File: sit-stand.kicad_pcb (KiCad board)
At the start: 2 copper layers, 160 x 50.8 mm, 63 parts, among them J1 USB_OTG, J2 CONN_02X03, J3 CONN_01X04, J4 CONN_01X16, J5 CONN_01X06, J6 CONN_02X04, U1 APA102, U10 APA102, U11 APA102, U12 APA102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

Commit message: clean up board
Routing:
- net +5V: track 453.1 -> 499.7 mm
- net GND: track 578.4 -> 573.6 mm, vias 24 -> 22
- net USB_D-: track 90.0 -> 93.9 mm
- net USB_ID: track 79.2 -> 76.9 mm
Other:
- board size 160 x 50.8 mm -> 158.8 x 50.8 mm

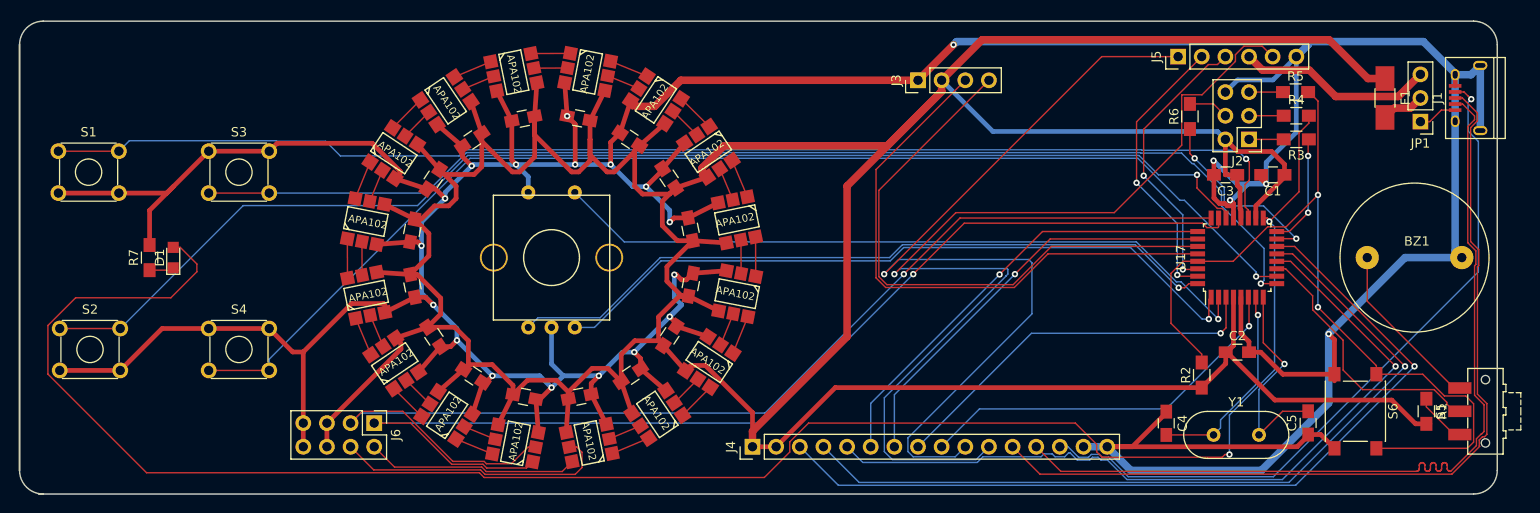
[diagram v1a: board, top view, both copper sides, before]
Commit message: shift oled and reroute led power
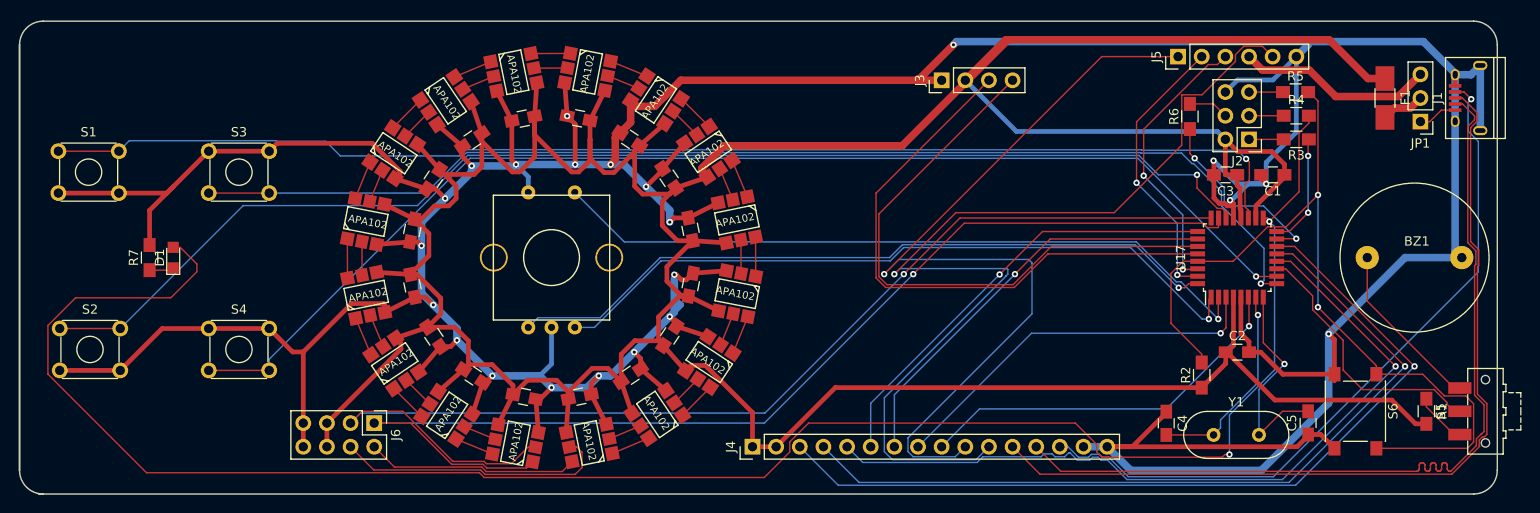
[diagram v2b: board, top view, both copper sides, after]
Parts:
- moved J3 2.54 mm to (168.9, 44.5)
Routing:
- net +5V: track 499.7 -> 456.6 mm
- net GND: track 573.6 -> 586.1 mm
- net OLED_SCL: track 61.7 -> 62.7 mm
- net OLED_SDA: track 62.3 -> 63.4 mm
- net Net-(S5-Pad2): track 28.9 -> 28.3 mm

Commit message: use thicker led power traces
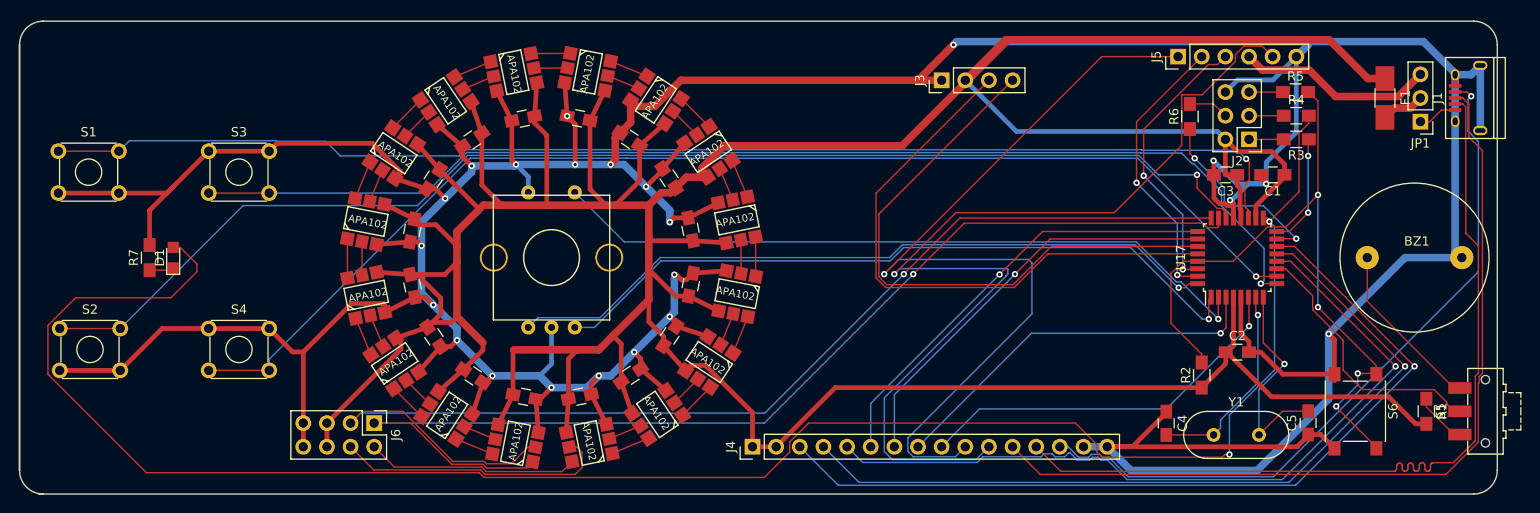
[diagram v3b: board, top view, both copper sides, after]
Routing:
- net +5V: track 456.6 -> 483.3 mm
- net RESET: track 91.1 -> 77.3 mm, vias 2 -> 4
- net GND: track 586.1 -> 573.7 mm
- net USB_D+: track 93.1 -> 91.5 mm
- net USB_D-: track 93.9 -> 92.3 mm

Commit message: added mounting holes
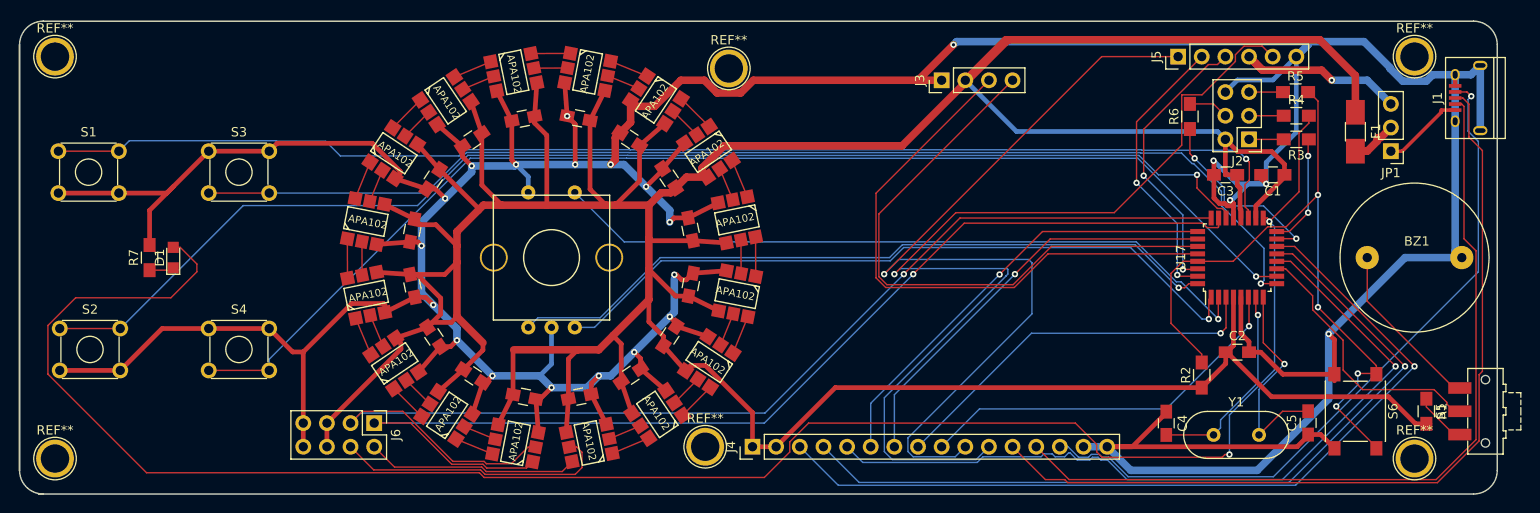
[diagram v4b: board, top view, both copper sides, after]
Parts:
- added REF**: 1pin, Connectors:1pin, F.Cu at (219.7, 41.9)
- added REF**: 1pin, Connectors:1pin, F.Cu at (143.5, 83.8)
- added REF**: 1pin, Connectors:1pin, F.Cu at (219.7, 85.1)
- added REF**: 1pin, Connectors:1pin, F.Cu at (146.1, 43.2)
- added REF**: 1pin, Connectors:1pin, F.Cu at (73.7, 85.1)
- added REF**: 1pin, Connectors:1pin, F.Cu at (73.7, 41.9)
- moved F1 4.82 mm to (213.4, 50.0)
- moved JP1 4.49 mm to (217.2, 52.1)
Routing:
- net Net-(J1-Pad1): track 4.24 -> 8.87 mm
- net USB_D-: track 92.3 -> 88.6 mm
- net SER_VCC: track 21.2 -> 19.4 mm, vias 0 -> 1
- net GND: track 573.7 -> 575.4 mm
- net USB_D+: track 91.5 -> 92.3 mm
- net +5V: track 483.3 -> 483.9 mm

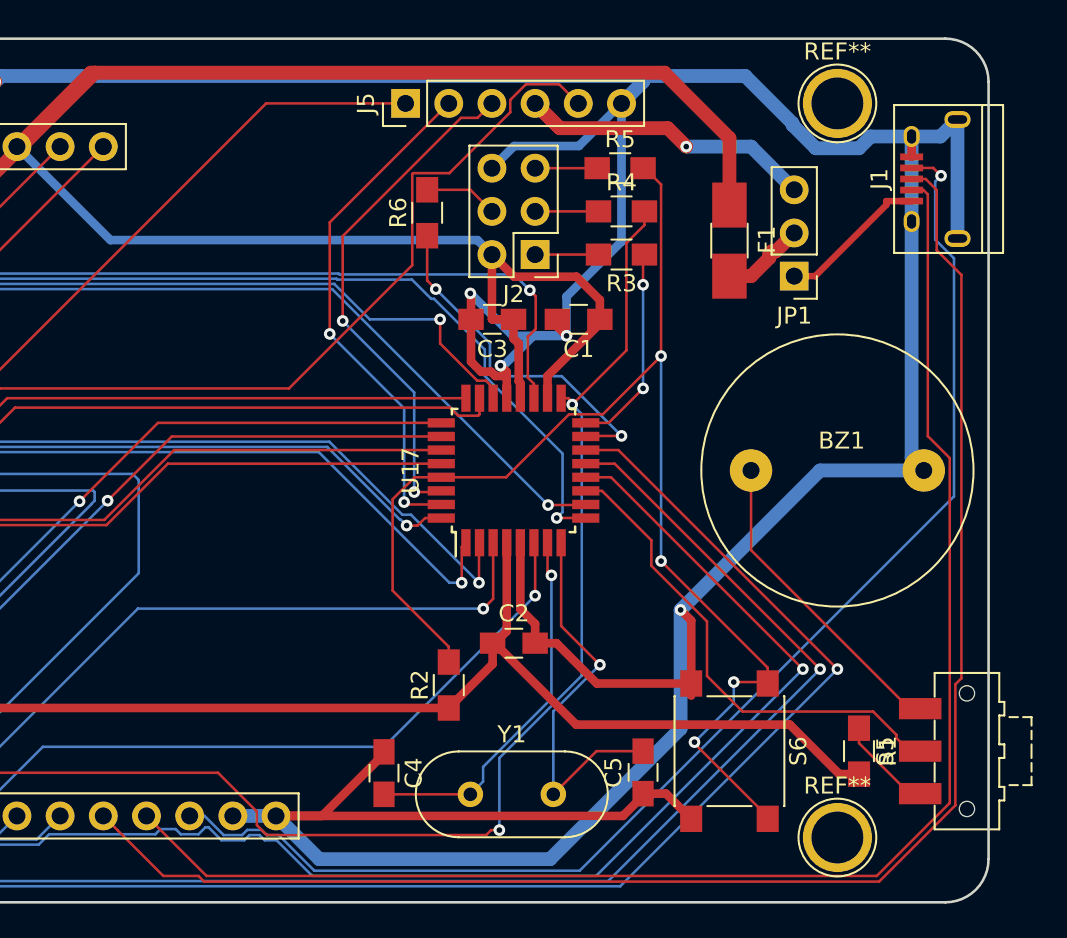
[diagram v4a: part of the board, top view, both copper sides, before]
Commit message: fixed differentials
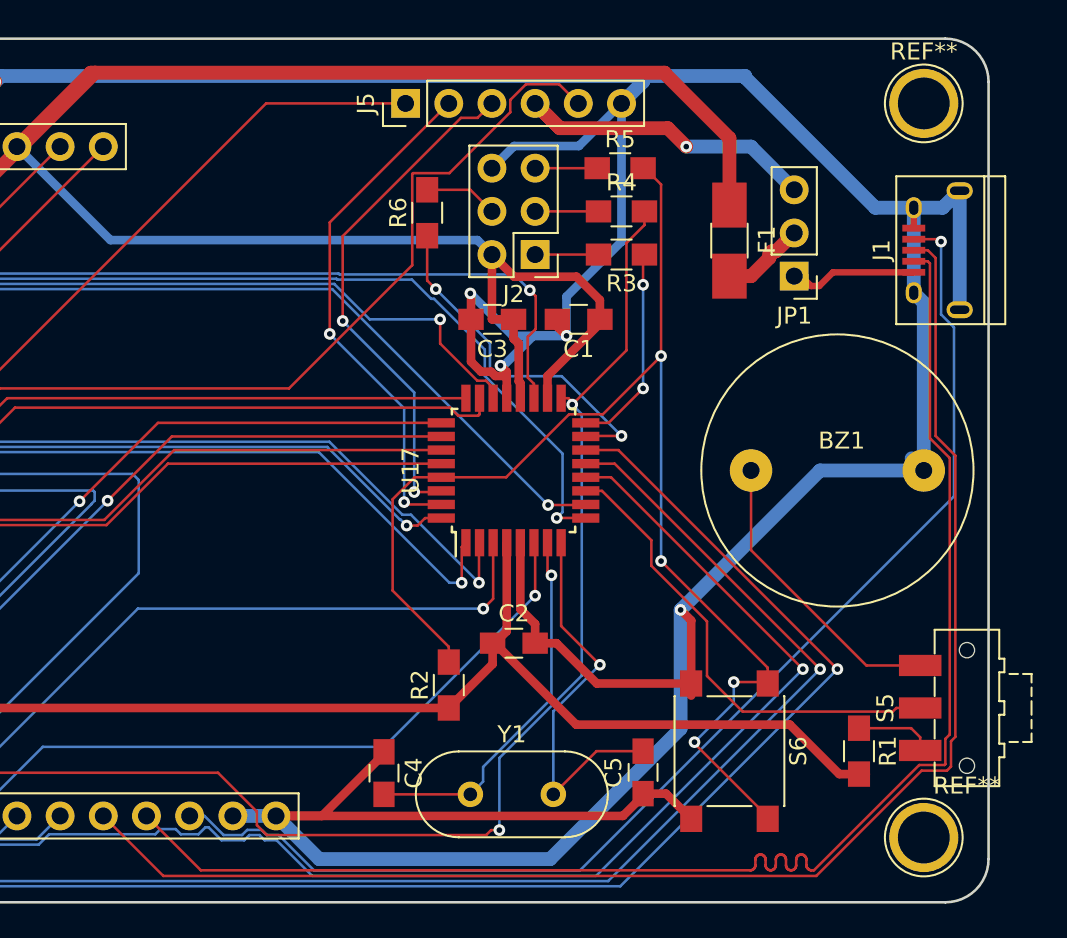
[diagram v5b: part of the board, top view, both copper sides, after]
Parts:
- moved REF** 5.08 mm to (224.8, 41.9)
- moved REF** 5.08 mm to (224.8, 85.1)
- moved J1 4.19 mm to (225.6, 50.5)
- moved S5 2.54 mm to (227.3, 77.5)
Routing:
- net USB_D+: track 92.3 -> 86.0 mm
- net USB_ID: track 77.0 -> 72.6 mm
- net GND: track 575.4 -> 573.5 mm
- net USB_D-: track 88.6 -> 86.7 mm
- net Net-(J1-Pad1): track 8.87 -> 7.53 mm
- net Net-(R1-Pad1): track 5.71 -> 4.60 mm
- net Net-(BZ1-Pad1): track 18.5 -> 17.4 mm

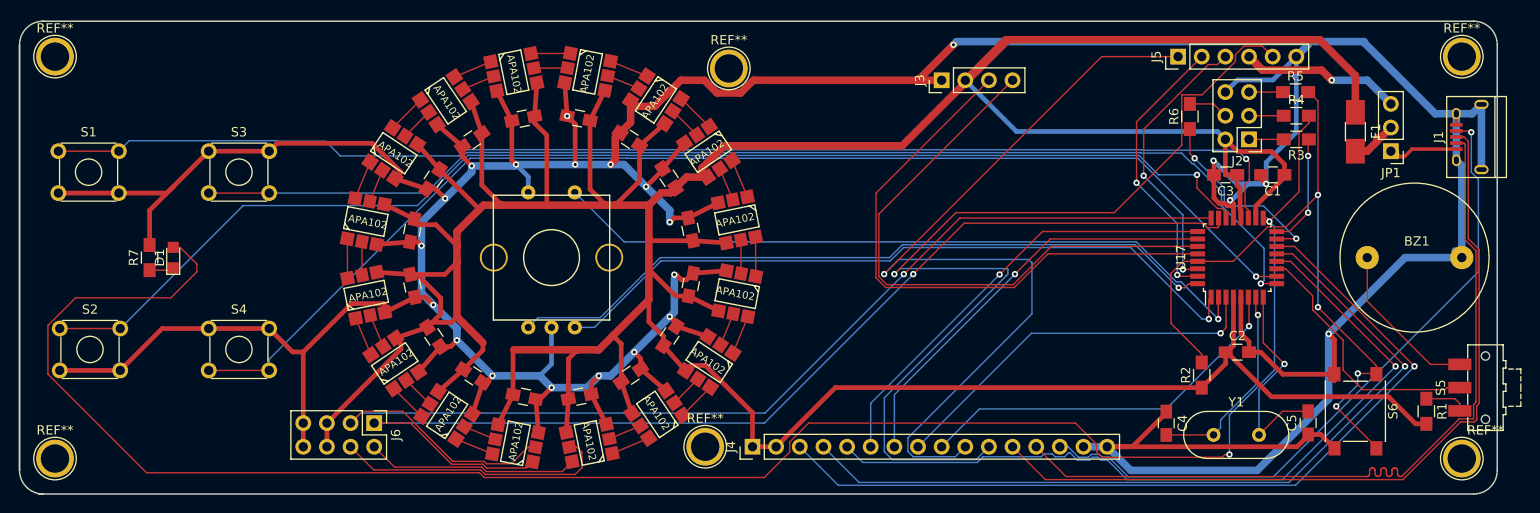
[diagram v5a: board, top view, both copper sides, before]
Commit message: fixed mounting holes positions
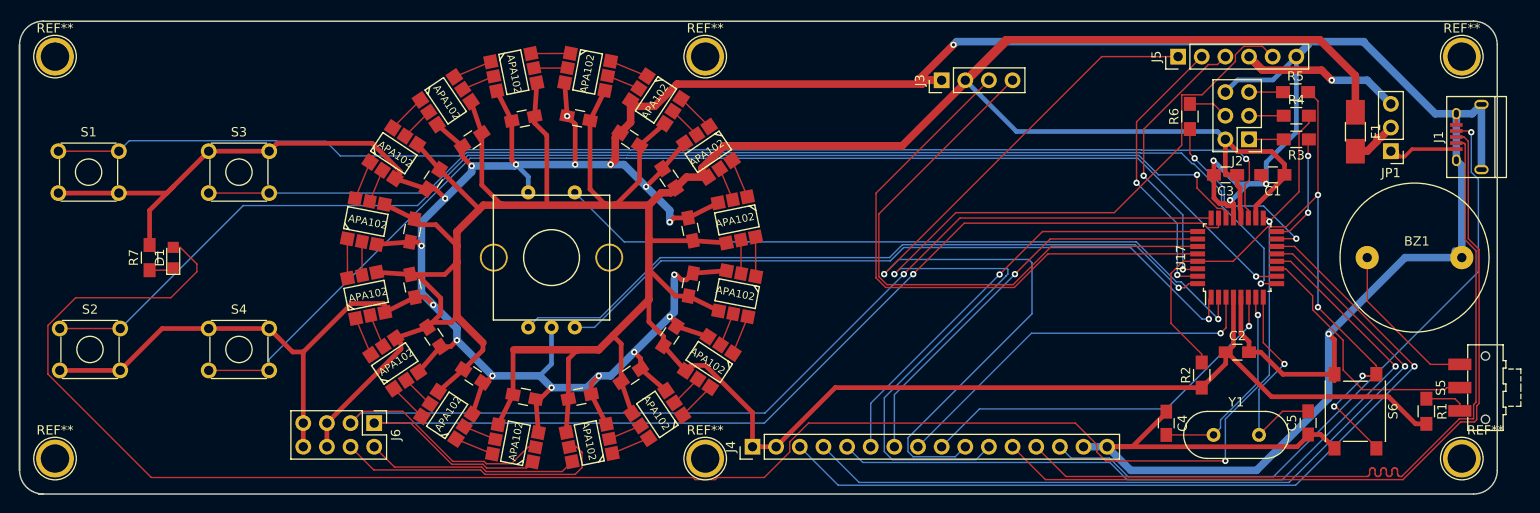
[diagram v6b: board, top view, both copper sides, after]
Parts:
- moved REF** 2.84 mm to (143.5, 41.9)
- moved REF** 1.27 mm to (143.5, 85.1)
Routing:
- net GND: track 573.5 -> 574.8 mm
- net PB0: track 84.2 -> 82.9 mm
- net RESET: track 77.3 -> 78.5 mm

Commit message: add ground and power planes
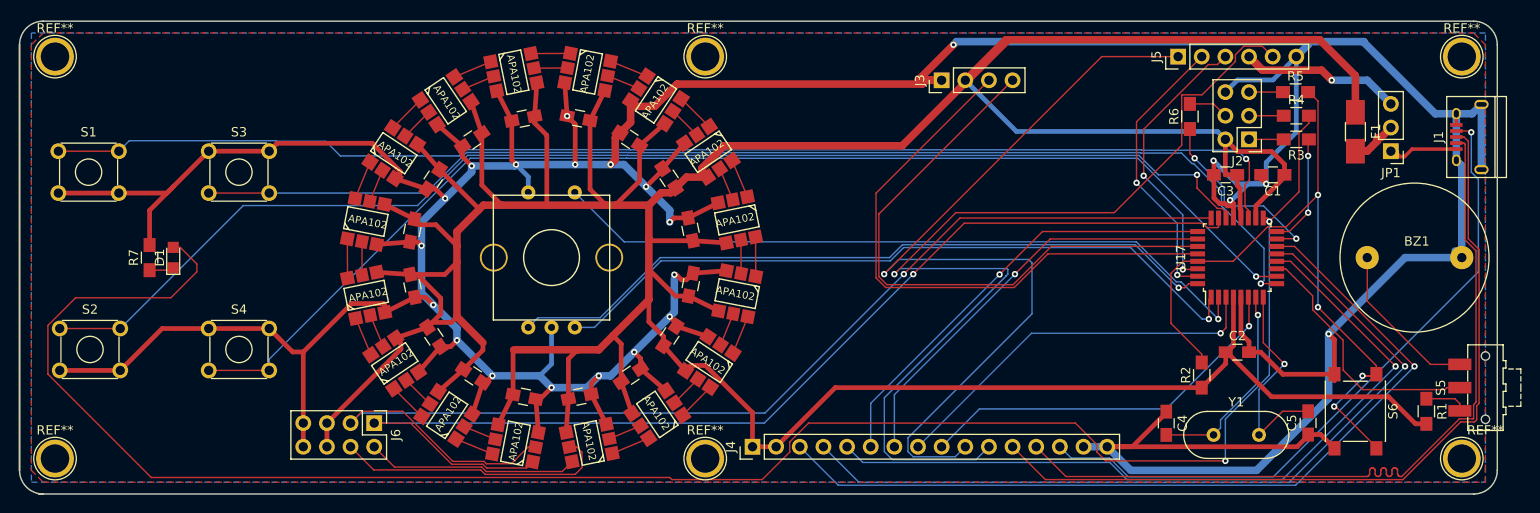
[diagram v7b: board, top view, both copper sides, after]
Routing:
- added copper zone on B.Cu, net +5V
- added copper zone on F.Cu, net GND
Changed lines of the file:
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@@
     (thickness 1.6002)
     (drawings 16)
-    (tracks 881)
+    (tracks 879)
     (zones 0)
     (modules 69)
@@
   (segment (start 203 82.55) (end 205.54 80.01) (width 0.1524) (layer F.Cu) (net 5) (status 10))
   (segment (start 205.54 80.01) (end 208.28 80.01) (width 0.1524) (layer F.Cu) (net 5) (status 20))
-  (segment (start 87.1124 62.4) (end 88.9 64.1876) (width 0.1524) (layer F.Cu) (net 6))
   (segment (start 86.36 62.4) (end 87.1124 62.4) (width 0.1524) (layer F.Cu) (net 6))
-  (segment (start 88.9 64.1876) (end 88.9 65.024) (width 0.1524) (layer F.Cu) (net 6))
-  (segment (start 149.86 87.122) (end 152.591399 84.390601) (width 0.1524) (layer F.Cu) (net 6))
-  (segment (start 144.82369 87.122) (end 149.86 87.122) (width 0.1524) (layer F.Cu) (net 6))
-  (segment (start 72.898 76.016778) (end 84.003222 87.122) (width 0.1524) (layer F.Cu) (net 6))
   (segment (start 72.898 70.79367) (end 72.898 76.016778) (width 0.1524) (layer F.Cu) (net 6))
-  (segment (start 142.19631 87.122) (end 142.424911 87.350601) (width 0.1524) (layer F.Cu) (net 6))
-  (segment (start 84.003222 87.122) (end 142.19631 87.122) (width 0.1524) (layer F.Cu) (net 6))
+  (segment (start 87.1124 62.4) (end 88.9 64.1876) (width 0.1524) (layer F.Cu) (net 6))
+  (segment (start 185.563799 83.567021) (end 185.563799 84.360577) (width 0.1524) (layer F.Cu) (net 6))
+  (segment (start 88.9 64.1876) (end 88.9 65.024) (width 0.1524) (layer F.Cu) (net 6))
+  (segment (start 139.928601 87.350601) (end 149.631399 87.350601) (width 0.1524) (layer F.Cu) (net 6))
   (segment (start 88.9 65.024) (end 86.106 67.818) (width 0.1524) (layer F.Cu) (net 6))
+  (segment (start 185.563799 84.360577) (end 186.547222 85.344) (width 0.1524) (layer F.Cu) (net 6))
+  (segment (start 154.61367 81.28) (end 183.276778 81.28) (width 0.1524) (layer F.Cu) (net 6))
   (segment (start 86.106 67.818) (end 75.87367 67.818) (width 0.1524) (layer F.Cu) (net 6))
+  (segment (start 183.276778 81.28) (end 185.563799 83.567021) (width 0.1524) (layer F.Cu) (net 6))
   (segment (start 75.87367 67.818) (end 72.898 70.79367) (width 0.1524) (layer F.Cu) (net 6))
-  (segment (start 142.424911 87.350601) (end 144.595089 87.350601) (width 0.1524) (layer F.Cu) (net 6))
-  (segment (start 152.591399 83.302271) (end 154.61367 81.28) (width 0.1524) (layer F.Cu) (net 6))
   (segment (start 152.591399 84.390601) (end 152.591399 83.302271) (width 0.1524) (layer F.Cu) (net 6))
-  (segment (start 144.595089 87.350601) (end 144.82369 87.122) (width 0.1524) (layer F.Cu) (net 6))
-  (segment (start 154.61367 81.28) (end 183.276778 81.28) (width 0.1524) (layer F.Cu) (net 6))
-  (segment (start 183.276778 81.28) (end 185.563799 83.567021) (width 0.1524) (layer F.Cu) (net 6))
-  (segment (start 185.563799 84.360577) (end 186.547222 85.344) (width 0.1524) (layer F.Cu) (net 6))
-  (segment (start 185.563799 83.567021) (end 185.563799 84.360577) (width 0.1524) (layer F.Cu) (net 6))
+  (segment (start 72.898 76.016778) (end 84.003222 87.122) (width 0.1524) (layer F.Cu) (net 6))
+  (segment (start 84.003222 87.122) (end 139.7 87.122) (width 0.1524) (layer F.Cu) (net 6))
+  (segment (start 139.7 87.122) (end 139.928601 87.350601) (width 0.1524) (layer F.Cu) (net 6))
+  (segment (start 149.631399 87.350601) (end 152.591399 84.390601) (width 0.1524) (layer F.Cu) (net 6))
+  (segment (start 152.591399 83.302271) (end 154.61367 81.28) (width 0.1524) (layer F.Cu) (net 6))
   (segment (start 186.547222 85.344) (end 199.39 85.344) (width 0.1524) (layer F.Cu) (net 6))
   (segment (start 199.39 80.848934) (end 199.39 85.344) (width 0.1524) (layer B.Cu) (net 6))
@@
   (segment (start 224.58 77.51) (end 224.58 77.514) (width 0.1524) (layer F.Cu) (net 76) (status 30))
   (segment (start 223.955 77.51) (end 224.58 77.51) (width 0.1524) (layer F.Cu) (net 76) (status 30))
+  (zone (net 1) (net_name GND) (layer F.Cu) (hatch edge 0.508)
+    (connect_pads (clearance 0.508))
+    (min_thickness 0.254)
+    (fill yes (arc_segments 16) (thermal_gap 0.508) (thermal_bridge_width 0.508))
+    (polygon
+      (pts
+        (xy 71.12 40.64) (xy 71.12 86.36) (xy 72.39 87.63) (xy 227.33 87.63) (xy 227.33 86.36)
+        (xy 227.33 40.64) (xy 226.06 39.37) (xy 72.39 39.37)
+      )
+    )
+  )
+  (zone (net 3) (net_name +5V) (layer B.Cu) (hatch edge 0.508)
+    (connect_pads (clearance 0.508))
+    (min_thickness 0.254)
+    (fill yes (arc_segments 16) (thermal_gap 0.508) (thermal_bridge_width 0.508))
+    (polygon
+      (pts
+        (xy 71.12 39.37) (xy 71.12 87.63) (xy 227.33 87.63) (xy 227.33 39.37)
+      )
+    )
+  )
 )
